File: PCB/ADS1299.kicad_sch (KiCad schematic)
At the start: 36 parts, among them CN2 W2A41C681KAT2A, CN5 W2A41C681KAT2A, CN6 W2A41C681KAT2A, CN7 W2A41C681KAT2A, U1 ADS1299IPAGR, U3 TPD4E1B06DCKR, U4 TPD4E1B06DCKR, U9 TPD4E1B06DCKR

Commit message: start of footprints
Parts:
- C1: footprint (none) -> Capacitor_SMD:C_0805_2012Metric_Pad1.18x1.45mm_HandSolder
- C10, C12, C14, C17, C4, C5, C9: footprint (none) -> Capacitor_SMD:C_0402_1005Metric_Pad0.74x0.62mm_HandSolder
- U1: footprint PAG64_TEX -> CustomLib:PAG64_TEX
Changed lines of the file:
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@@
 			)
 		)
-		(property "Footprint" ""
+		(property "Footprint" "Capacitor_SMD:C_0402_1005Metric_Pad0.74x0.62mm_HandSolder"
 			(at 98.7552 40.64 0)
 			(effects
@@
 			)
 		)
-		(property "Footprint" ""
+		(property "Footprint" "Capacitor_SMD:C_0402_1005Metric_Pad0.74x0.62mm_HandSolder"
 			(at 207.3148 120.65 0)
 			(effects
@@
 			)
 		)
-		(property "Footprint" ""
+		(property "Footprint" "Capacitor_SMD:C_0402_1005Metric_Pad0.74x0.62mm_HandSolder"
 			(at 112.7252 40.64 0)
 			(effects
@@
 			)
 		)
-		(property "Footprint" ""
+		(property "Footprint" "Capacitor_SMD:C_0402_1005Metric_Pad0.74x0.62mm_HandSolder"
 			(at 218.1352 128.27 0)
 			(effects
@@
 			)
 		)
-		(property "Footprint" ""
+		(property "Footprint" "Capacitor_SMD:C_0805_2012Metric_Pad1.18x1.45mm_HandSolder"
 			(at 176.53 26.3652 0)
 			(effects
@@
 			)
 		)
-		(property "Footprint" ""
+		(property "Footprint" "Capacitor_SMD:C_0402_1005Metric_Pad0.74x0.62mm_HandSolder"
 			(at 140.6652 40.64 0)
 			(effects
@@
 			)
 		)
-		(property "Footprint" ""
+		(property "Footprint" "Capacitor_SMD:C_0402_1005Metric_Pad0.74x0.62mm_HandSolder"
 			(at 126.6952 40.64 0)
 			(effects
@@
 			)
 		)
-		(property "Footprint" "PAG64_TEX"
+		(property "Footprint" "CustomLib:PAG64_TEX"
 			(at 202.692 74.676 0)
 			(effects
@@
 			)
 		)
-		(property "Footprint" ""
+		(property "Footprint" "Capacitor_SMD:C_0402_1005Metric_Pad0.74x0.62mm_HandSolder"
 			(at 195.2752 128.27 0)
 			(effects

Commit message: more footprints
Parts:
- C3: footprint (none) -> Capacitor_SMD:C_0805_2012Metric_Pad1.18x1.45mm_HandSolder
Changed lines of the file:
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@@
 			)
 		)
-		(property "Footprint" ""
+		(property "Footprint" "Capacitor_SMD:C_0805_2012Metric_Pad1.18x1.45mm_HandSolder"
 			(at 187.6552 128.27 0)
 			(effects

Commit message: cap footprints finished
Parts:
- C11, C15, C16, C2, C6, C7, C8: footprint (none) -> Capacitor_SMD:C_0603_1608Metric_Pad1.08x0.95mm_HandSolder
- C13: footprint (none) -> Capacitor_SMD:C_1210_3225Metric_Pad1.33x2.70mm_HandSolder
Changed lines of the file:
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@@
 			)
 		)
-		(property "Footprint" ""
+		(property "Footprint" "Capacitor_SMD:C_0603_1608Metric_Pad1.08x0.95mm_HandSolder"
 			(at 179.3748 120.65 0)
 			(effects
@@
 			)
 		)
-		(property "Footprint" ""
+		(property "Footprint" "Capacitor_SMD:C_1210_3225Metric_Pad1.33x2.70mm_HandSolder"
 			(at 227.0252 128.27 0)
 			(effects
@@
 			)
 		)
-		(property "Footprint" ""
+		(property "Footprint" "Capacitor_SMD:C_0603_1608Metric_Pad1.08x0.95mm_HandSolder"
 			(at 200.9648 120.65 0)
 			(effects
@@
 			)
 		)
-		(property "Footprint" ""
+		(property "Footprint" "Capacitor_SMD:C_0603_1608Metric_Pad1.08x0.95mm_HandSolder"
 			(at 134.3152 40.64 0)
 			(effects
@@
 			)
 		)
-		(property "Footprint" ""
+		(property "Footprint" "Capacitor_SMD:C_0603_1608Metric_Pad1.08x0.95mm_HandSolder"
 			(at 133.0452 80.01 0)
 			(effects
@@
 			)
 		)
-		(property "Footprint" ""
+		(property "Footprint" "Capacitor_SMD:C_0603_1608Metric_Pad1.08x0.95mm_HandSolder"
 			(at 120.3452 40.64 0)
 			(effects
@@
 			)
 		)
-		(property "Footprint" ""
+		(property "Footprint" "Capacitor_SMD:C_0603_1608Metric_Pad1.08x0.95mm_HandSolder"
 			(at 106.3752 40.64 0)
 			(effects
@@
 			)
 		)
-		(property "Footprint" ""
+		(property "Footprint" "Capacitor_SMD:C_0603_1608Metric_Pad1.08x0.95mm_HandSolder"
 			(at 148.2852 40.64 0)
 			(effects

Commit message: cap and resis array footprints
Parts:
- CN2, CN5, CN6, CN7: footprint W2A41C681KAT2A:CAPCAXE50P210X130X94-8N -> CustomLib:W3A41C102MAT2A
- RN5, RN6, RN7, RN8: footprint CAY16-103J4LF:RESCAF80P320X160X60-8N -> CustomLib:CAT16A203J4LF
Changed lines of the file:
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@@
 			)
 		)
-		(property "Footprint" "CAY16-103J4LF:RESCAF80P320X160X60-8N"
+		(property "Footprint" "CustomLib:CAT16A203J4LF"
 			(at 119.38 158.75 0)
 			(effects
@@
 			)
 		)
-		(property "Footprint" "W2A41C681KAT2A:CAPCAXE50P210X130X94-8N"
+		(property "Footprint" "CustomLib:W3A41C102MAT2A"
 			(at 64.77 118.11 0)
 			(effects
@@
 			)
 		)
-		(property "Footprint" "W2A41C681KAT2A:CAPCAXE50P210X130X94-8N"
+		(property "Footprint" "CustomLib:W3A41C102MAT2A"
 			(at 138.43 176.53 0)
 			(effects
@@
 			)
 		)
-		(property "Footprint" "W2A41C681KAT2A:CAPCAXE50P210X130X94-8N"
+		(property "Footprint" "CustomLib:W3A41C102MAT2A"
 			(at 64.77 176.53 0)
 			(effects
@@
 			)
 		)
-		(property "Footprint" "W2A41C681KAT2A:CAPCAXE50P210X130X94-8N"
+		(property "Footprint" "CustomLib:W3A41C102MAT2A"
 			(at 64.77 59.69 0)
 			(effects
@@
 			)
 		)
-		(property "Footprint" "CAY16-103J4LF:RESCAF80P320X160X60-8N"
+		(property "Footprint" "CustomLib:CAT16A203J4LF"
 			(at 45.72 158.75 0)
 			(effects
@@
 			)
 		)
-		(property "Footprint" "CAY16-103J4LF:RESCAF80P320X160X60-8N"
+		(property "Footprint" "CustomLib:CAT16A203J4LF"
 			(at 45.72 100.33 0)
 			(effects
@@
 			)
 		)
-		(property "Footprint" "CAY16-103J4LF:RESCAF80P320X160X60-8N"
+		(property "Footprint" "CustomLib:CAT16A203J4LF"
 			(at 45.72 41.91 0)
 			(effects

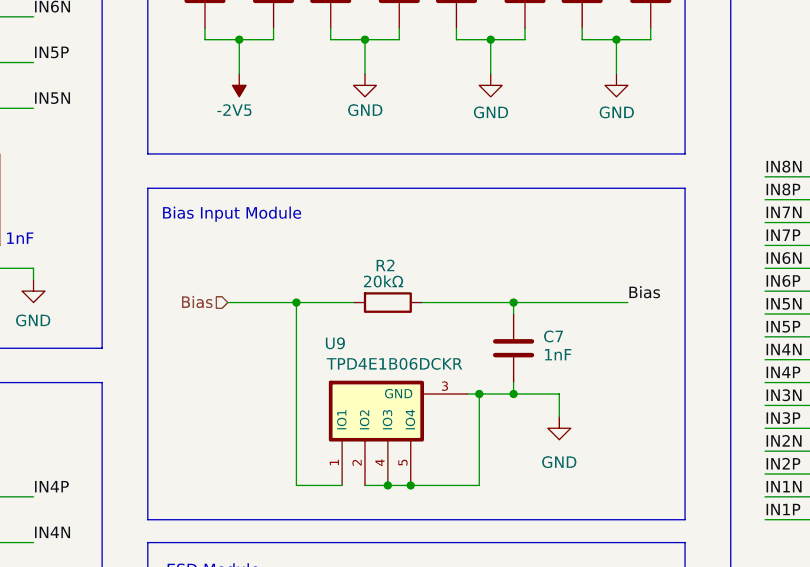
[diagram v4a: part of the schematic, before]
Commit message: res footprints
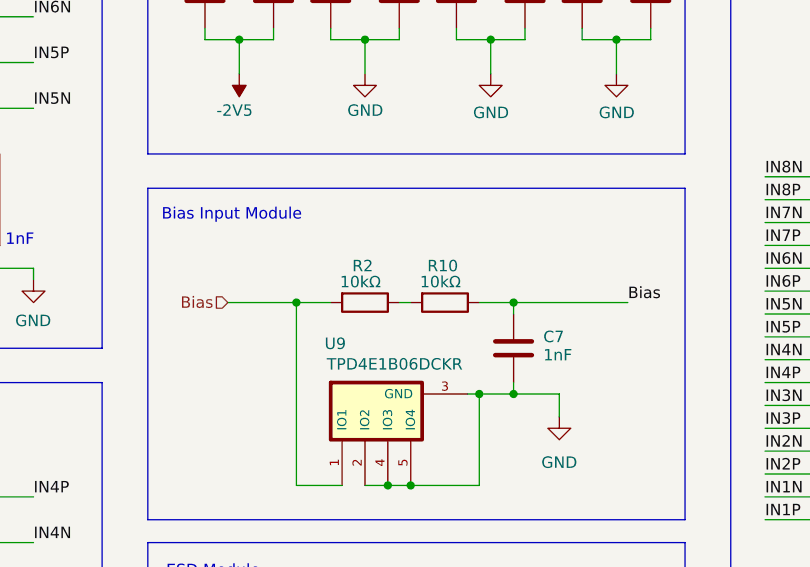
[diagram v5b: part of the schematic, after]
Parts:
- added R10: 10kΩ, Resistor_SMD:R_0805_2012Metric_Pad1.20x1.40mm_HandSolder, symbol Device:R
- R1: footprint (none) -> Resistor_SMD:R_0402_1005Metric_Pad0.72x0.64mm_HandSolder
- R2: value 20kΩ -> 10kΩ; footprint (none) -> Resistor_SMD:R_0805_2012Metric_Pad1.20x1.40mm_HandSolder
- R3, R6, R7, R8, R9: footprint (none) -> Resistor_SMD:R_0805_2012Metric_Pad1.20x1.40mm_HandSolder
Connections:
- net Bias: now also R10.1; no longer R2.1
- new net: R10.2, R2.1
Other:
- moved on the sheet: R2
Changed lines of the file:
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@@
 	)
 	(junction
+		(at 132.08 71.12)
+		(diameter 0)
+		(color 0 0 0 0)
+	)
+	(junction
 		(at 175.26 34.29)
 		(diameter 0)
@@
 	)
 	(junction
-		(at 132.08 71.12)
-		(diameter 0)
-		(color 0 0 0 0)
-	)
-	(junction
 		(at 203.2 38.1)
 		(diameter 0)
@@
 	(wire
 		(pts
-			(xy 107.95 71.12) (xy 114.3 71.12)
+			(xy 107.95 71.12) (xy 111.76 71.12)
 		)
 		(stroke
@@
 	(wire
 		(pts
+			(xy 128.27 71.12) (xy 132.08 71.12)
+		)
+		(stroke
+			(width 0)
+			(type default)
+		)
+	)
+	(wire
+		(pts
 			(xy 133.35 30.48) (xy 133.35 33.02)
 		)
@@
 	(wire
 		(pts
+			(xy 119.38 71.12) (xy 120.65 71.12)
+		)
+		(stroke
+			(width 0)
+			(type default)
+		)
+	)
+	(wire
+		(pts
 			(xy 55.88 156.21) (xy 67.31 156.21)
 		)
@@
 	(wire
 		(pts
-			(xy 121.92 71.12) (xy 132.08 71.12)
-		)
-		(stroke
-			(width 0)
-			(type default)
-		)
-	)
-	(wire
-		(pts
 			(xy 130.81 184.15) (xy 135.89 184.15)
 		)
@@
 	)
 	(symbol
+		(lib_id "Device:R")
+		(at 124.46 71.12 270)
+		(unit 1)
+		(exclude_from_sim no)
+		(in_bom yes)
+		(on_board yes)
+		(dnp no)
+		(property "Reference" "R10"
+			(at 124.206 67.056 90)
+			(effects
+				(font
+					(size 1.27 1.27)
+				)
+			)
+		)
+		(property "Value" "10kΩ"
+			(at 123.952 68.834 90)
+			(effects
+				(font
+					(size 1.27 1.27)
+				)
+			)
+		)
+		(property "Footprint" "Resistor_SMD:R_0805_2012Metric_Pad1.20x1.40mm_HandSolder"
+			(at 124.46 69.342 90)
+			(effects
+				(font
+					(size 1.27 1.27)
+				)
+				(hide yes)
+			)
+		)
+		(property "Datasheet" "~"
+			(at 124.46 71.12 0)
+			(effects
+				(font
+					(size 1.27 1.27)
+				)
+				(hide yes)
+			)
+		)
+		(property "Description" "Resistor"
+			(at 124.46 71.12 0)
+			(effects
+				(font
+					(size 1.27 1.27)
+				)
+				(hide yes)
+			)
+		)
+		(pin "1"
+		)
+		(pin "2"
+		)
+		(instances
+			(project "PCBs"
+				(path "/5beccadf-d27e-4f5e-8faf-404ef06d8def/3a403ee7-d625-4b59-9159-055fbed092ab"
+					(reference "R10")
+					(unit 1)
+				)
+			)
+		)
+	)
+	(symbol
 		(lib_id "custom_lib:CAY16-103J4LF")
 		(at 119.38 158.75 0)
@@
 			)
 		)
-		(property "Footprint" ""
+		(property "Footprint" "Resistor_SMD:R_0805_2012Metric_Pad1.20x1.40mm_HandSolder"
 			(at 263.652 99.06 90)
 			(effects
@@
 			)
 		)
-		(property "Footprint" ""
+		(property "Footprint" "Resistor_SMD:R_0805_2012Metric_Pad1.20x1.40mm_HandSolder"
 			(at 245.872 99.06 90)
 			(effects
@@
 			)
 		)
-		(property "Footprint" ""
+		(property "Footprint" "Resistor_SMD:R_0805_2012Metric_Pad1.20x1.40mm_HandSolder"
 			(at 239.522 55.88 90)
 			(effects
@@
 			)
 		)
-		(property "Footprint" ""
+		(property "Footprint" "Resistor_SMD:R_0805_2012Metric_Pad1.20x1.40mm_HandSolder"
 			(at 236.982 99.06 90)
 			(effects
@@
 	(symbol
 		(lib_id "Device:R")
-		(at 118.11 71.12 270)
+		(at 115.57 71.12 270)
 		(unit 1)
 		(exclude_from_sim no)
@@
 		(dnp no)
 		(property "Reference" "R2"
-			(at 117.856 67.056 90)
+			(at 115.316 67.056 90)
 			(effects
 				(font
@@
 			)
 		)
-		(property "Value" "20kΩ"
-			(at 117.602 68.834 90)
+		(property "Value" "10kΩ"
+			(at 115.062 68.834 90)
 			(effects
 				(font
@@
 			)
 		)
-		(property "Footprint" ""
-			(at 118.11 69.342 90)
+		(property "Footprint" "Resistor_SMD:R_0805_2012Metric_Pad1.20x1.40mm_HandSolder"
+			(at 115.57 69.342 90)
 			(effects
 				(font
@@
 		)
 		(property "Datasheet" "~"
-			(at 118.11 71.12 0)
+			(at 115.57 71.12 0)
 			(effects
 				(font
@@
 		)
 		(property "Description" "Resistor"
-			(at 118.11 71.12 0)
+			(at 115.57 71.12 0)
 			(effects
 				(font
@@
 			)
 		)
-		(property "Footprint" ""
+		(property "Footprint" "Resistor_SMD:R_0402_1005Metric_Pad0.72x0.64mm_HandSolder"
 			(at 180.34 32.512 90)
 			(effects
@@
 			)
 		)
-		(property "Footprint" ""
+		(property "Footprint" "Resistor_SMD:R_0805_2012Metric_Pad1.20x1.40mm_HandSolder"
 			(at 254.762 99.06 90)
 			(effects

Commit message: initial pcb import
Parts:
- U3, U4, U9: footprint TPD4E1B06DCKR:SOT65P210X110-6N -> CustomLib:tpd4e1b06dckr
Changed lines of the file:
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@@
 			)
 		)
-		(property "Footprint" "TPD4E1B06DCKR:SOT65P210X110-6N"
+		(property "Footprint" "CustomLib:tpd4e1b06dckr"
 			(at 112.522 145.034 0)
 			(effects
@@
 			)
 		)
-		(property "Footprint" "TPD4E1B06DCKR:SOT65P210X110-6N"
+		(property "Footprint" "CustomLib:tpd4e1b06dckr"
 			(at 135.382 145.034 0)
 			(effects
@@
 			)
 		)
-		(property "Footprint" "TPD4E1B06DCKR:SOT65P210X110-6N"
+		(property "Footprint" "CustomLib:tpd4e1b06dckr"
 			(at 122.682 113.284 0)
 			(effects
